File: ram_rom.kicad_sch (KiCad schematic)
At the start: 1 part

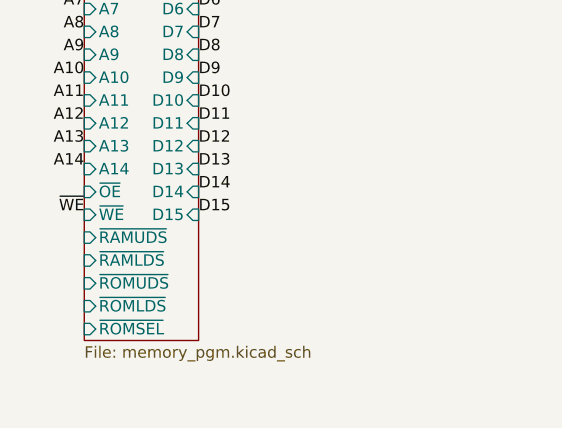
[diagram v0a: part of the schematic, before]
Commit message: Switch ROM chips to SRAM and add onboard programmer
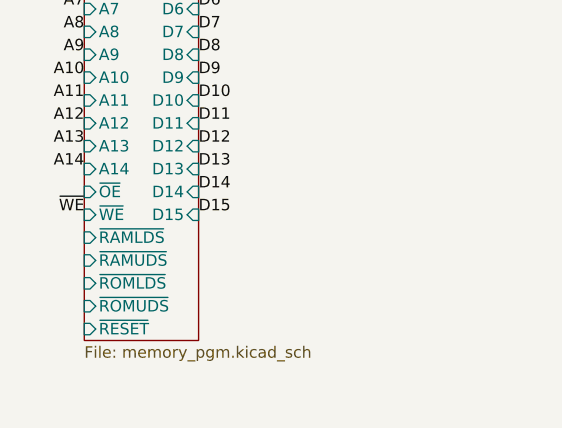
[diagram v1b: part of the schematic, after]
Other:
- sheet MemoryPgm ports: added ~{RESET}; removed ~{ROMSEL}

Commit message: Add title and rev number
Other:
- title: (none) -> RAM/ROM Board
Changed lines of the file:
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@@
 (kicad_sch (version 20211123) (generator eeschema)
   (paper "USLetter")
+  (title_block
+    (title "RAM/ROM Board")
+    (rev "1")
+  )
   (label "D9" (at 238.76 120.65 180)
     (effects (font (size 1.27 1.27)) (justify right bottom))

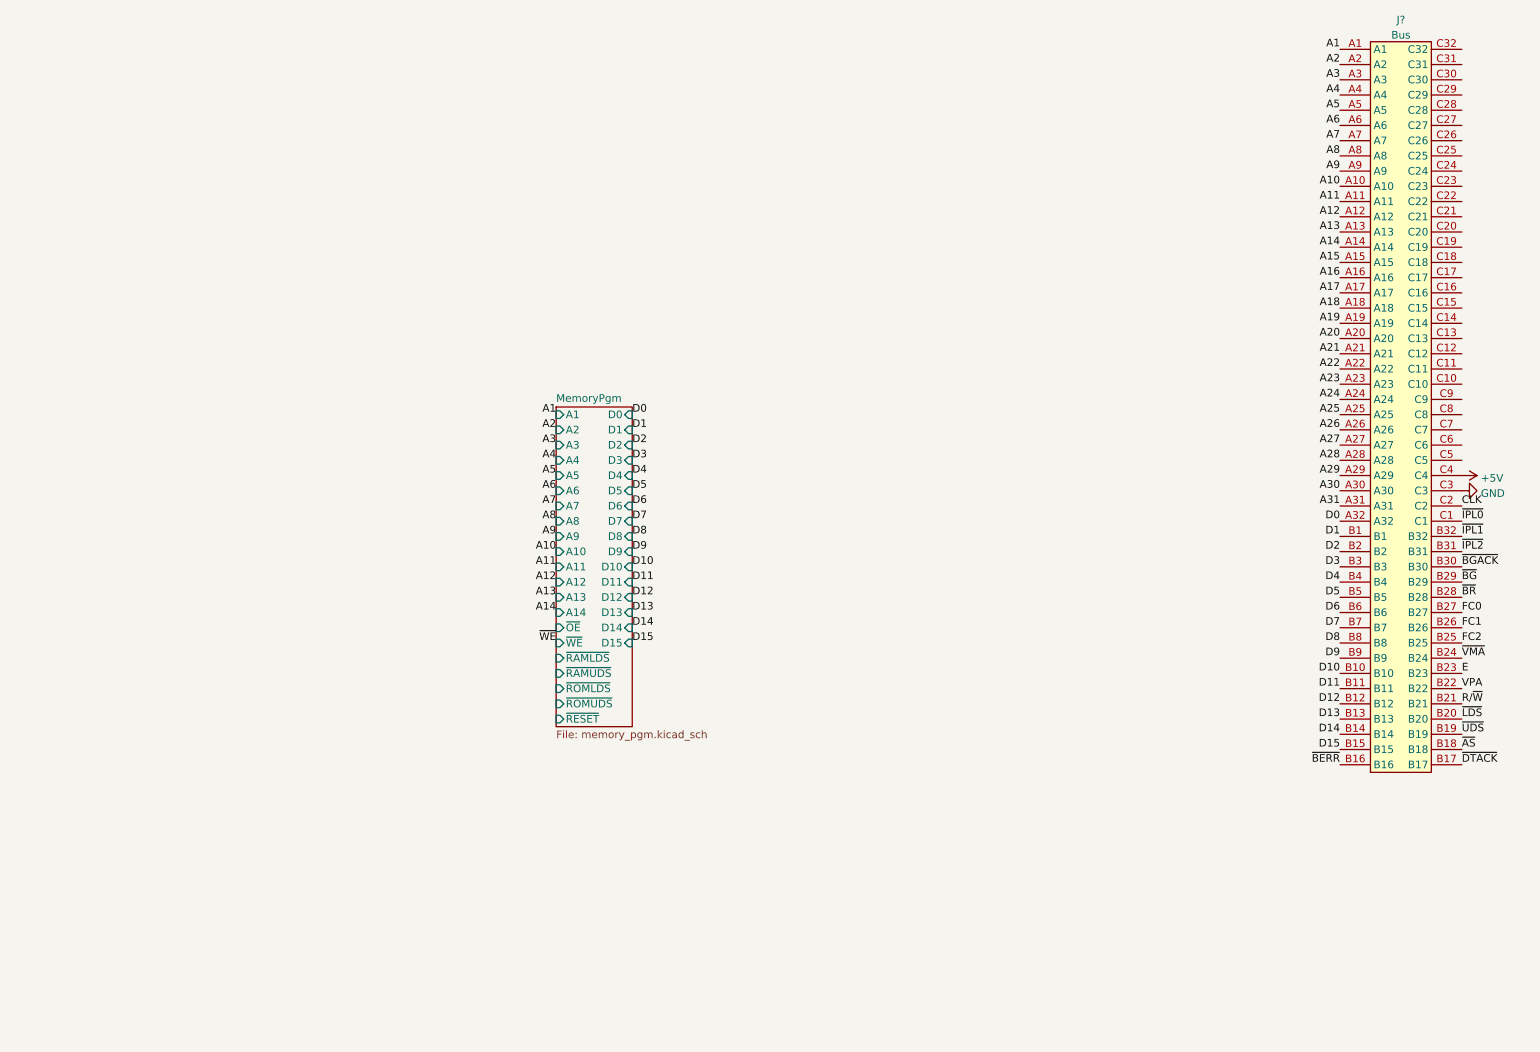
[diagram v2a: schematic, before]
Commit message: First pass at address decoding logic
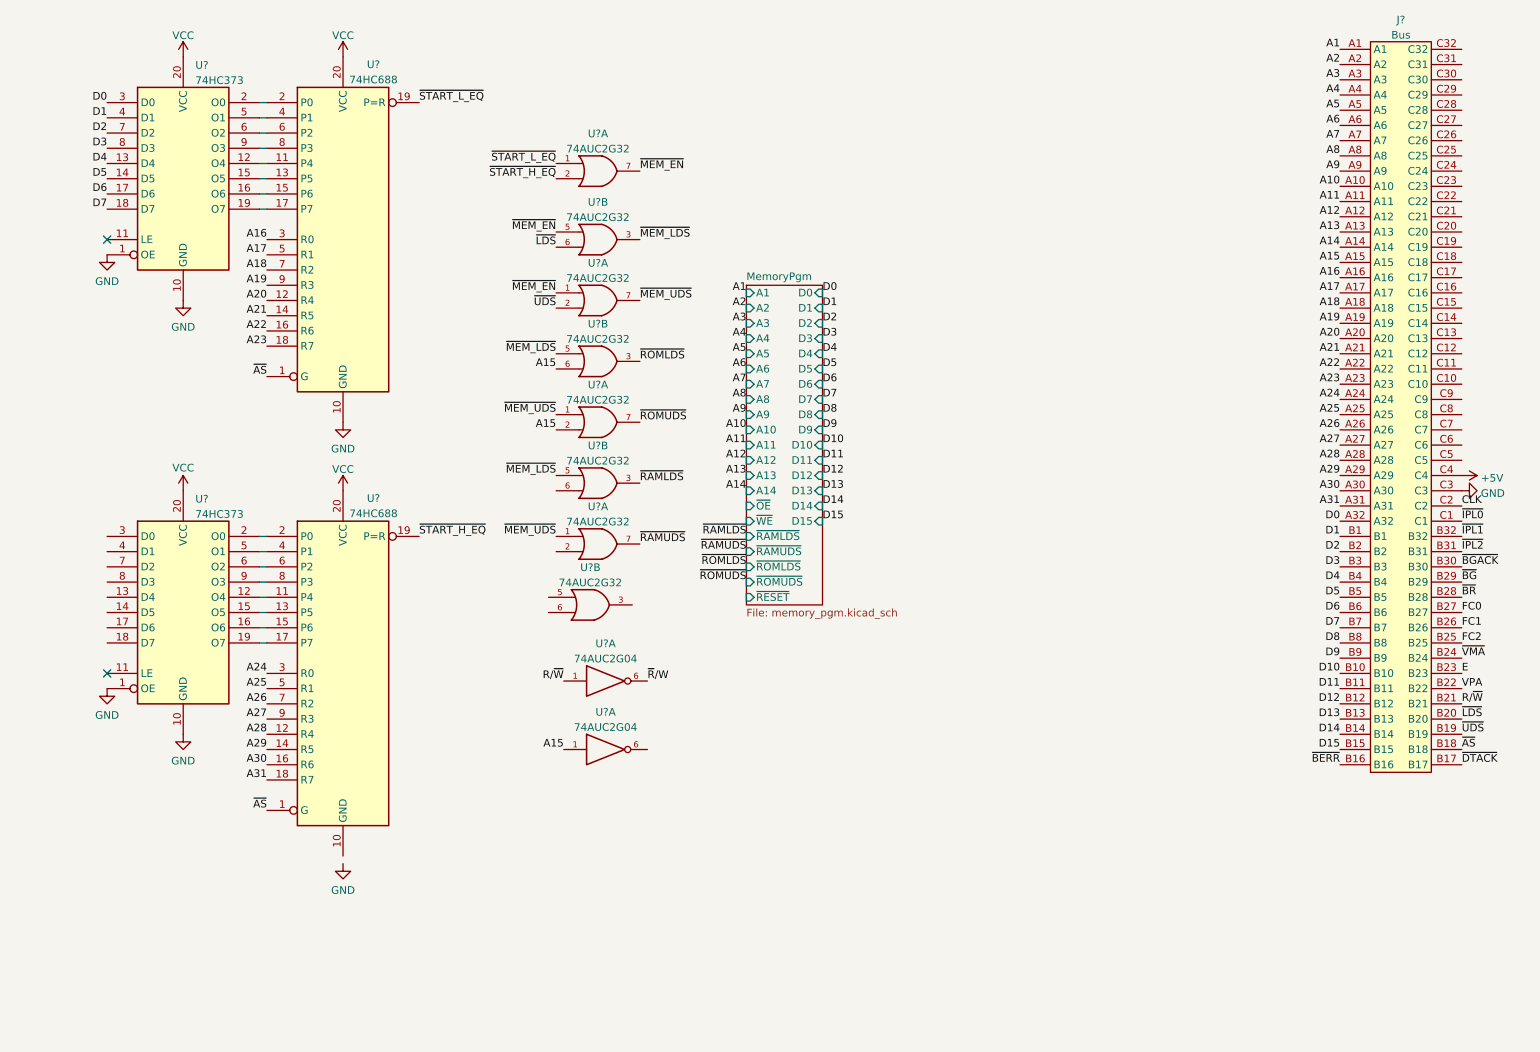
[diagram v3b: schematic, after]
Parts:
- added U? (x8): 74AUC2G32, symbol 74xGxx:74AUC2G32
- added U? (x2): 74AUC2G04, symbol 74xGxx:74AUC2G04
- added U? (x2): 74HC688, symbol 74xx:74HC688
- added U? (x2): 74HC373, symbol 74xx:74HC373
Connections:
- net A15: now also U?.1, U?.2, U?.6
- net A16: now also U?.3 (R0)
- net A17: now also U?.5 (R1)
- net A18: now also U?.7 (R2)
- net A19: now also U?.9 (R3)
- net A20: now also U?.12 (R4)
- net A21: now also U?.14 (R5)
- net A22: now also U?.16 (R6)
- net A23: now also U?.18 (R7)
- net A24: now also U?.3 (R0)
- net A25: now also U?.5 (R1)
- net A26: now also U?.7 (R2)
- net A27: now also U?.9 (R3)
- net A28: now also U?.12 (R4)
- net A29: now also U?.14 (R5)
- net A30: now also U?.16 (R6)
- net A31: now also U?.18 (R7)
- net D0: now also U?.3 (D0)
- net D1: now also U?.4 (D1)
- net D2: now also U?.7 (D2)
- net D3: now also U?.8 (D3)
- net D4: now also U?.13 (D4)
- net D5: now also U?.14 (D5)
- net D6: now also U?.17 (D6)
- net D7: now also U?.18 (D7)
- net GND: now also U?.1 (OE), U?.1 (OE), U?.10 (GND), U?.10 (GND), U?.10 (GND), U?.2 (GND), U?.2 (GND), U?.4 (GND), U?.4 (GND), U?.4 (GND), U?.4 (GND), U?.4 (GND), U?.4 (GND), U?.4 (GND), U?.4 (GND)
- net R/~{W}: now also U?.1
- net ~{AS}: now also U?.1 (G), U?.1 (G)
- net ~{LDS}: now also U?.6
- net ~{UDS}: now also U?.2
- new net: U?.11 (P4), U?.12 (O4) (x2)
- new net: U?.13 (P5), U?.15 (O5) (x2)
- new net: U?.15 (P6), U?.16 (O6) (x2)
- new net: U?.17 (P7), U?.19 (O7) (x2)
- new net: U?.2 (O0), U?.2 (P0) (x2)
- new net: U?.4 (P1), U?.5 (O1) (x2)
- new net: U?.6 (O2), U?.6 (P2) (x2)
- new net: U?.8 (P3), U?.9 (O3) (x2)
- new net VCC: U?.20 (VCC), U?.20 (VCC), U?.20 (VCC), U?.20 (VCC), U?.5 (VCC), U?.5 (VCC), U?.8 (VCC), U?.8 (VCC), U?.8 (VCC), U?.8 (VCC), U?.8 (VCC), U?.8 (VCC), U?.8 (VCC), U?.8 (VCC)
- new net ~{MEM_EN}: U?.1, U?.5, U?.7
- new net ~{MEM_LDS}: U?.3, U?.5, U?.5
- new net ~{MEM_UDS}: U?.1, U?.1, U?.7
- new net ~{RAMLDS}: U?.3
- new net ~{RAMUDS}: U?.7
- new net ~{ROMLDS}: U?.3
- new net ~{ROMUDS}: U?.7
- new net ~{R}/W: U?.6
- new net ~{START_H_EQ}: U?.19 (P=R), U?.2
- new net ~{START_L_EQ}: U?.1, U?.19 (P=R)
- no-connect marks 0 -> 2

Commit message: Consolidate RAM into one chip and work on adddress decoding
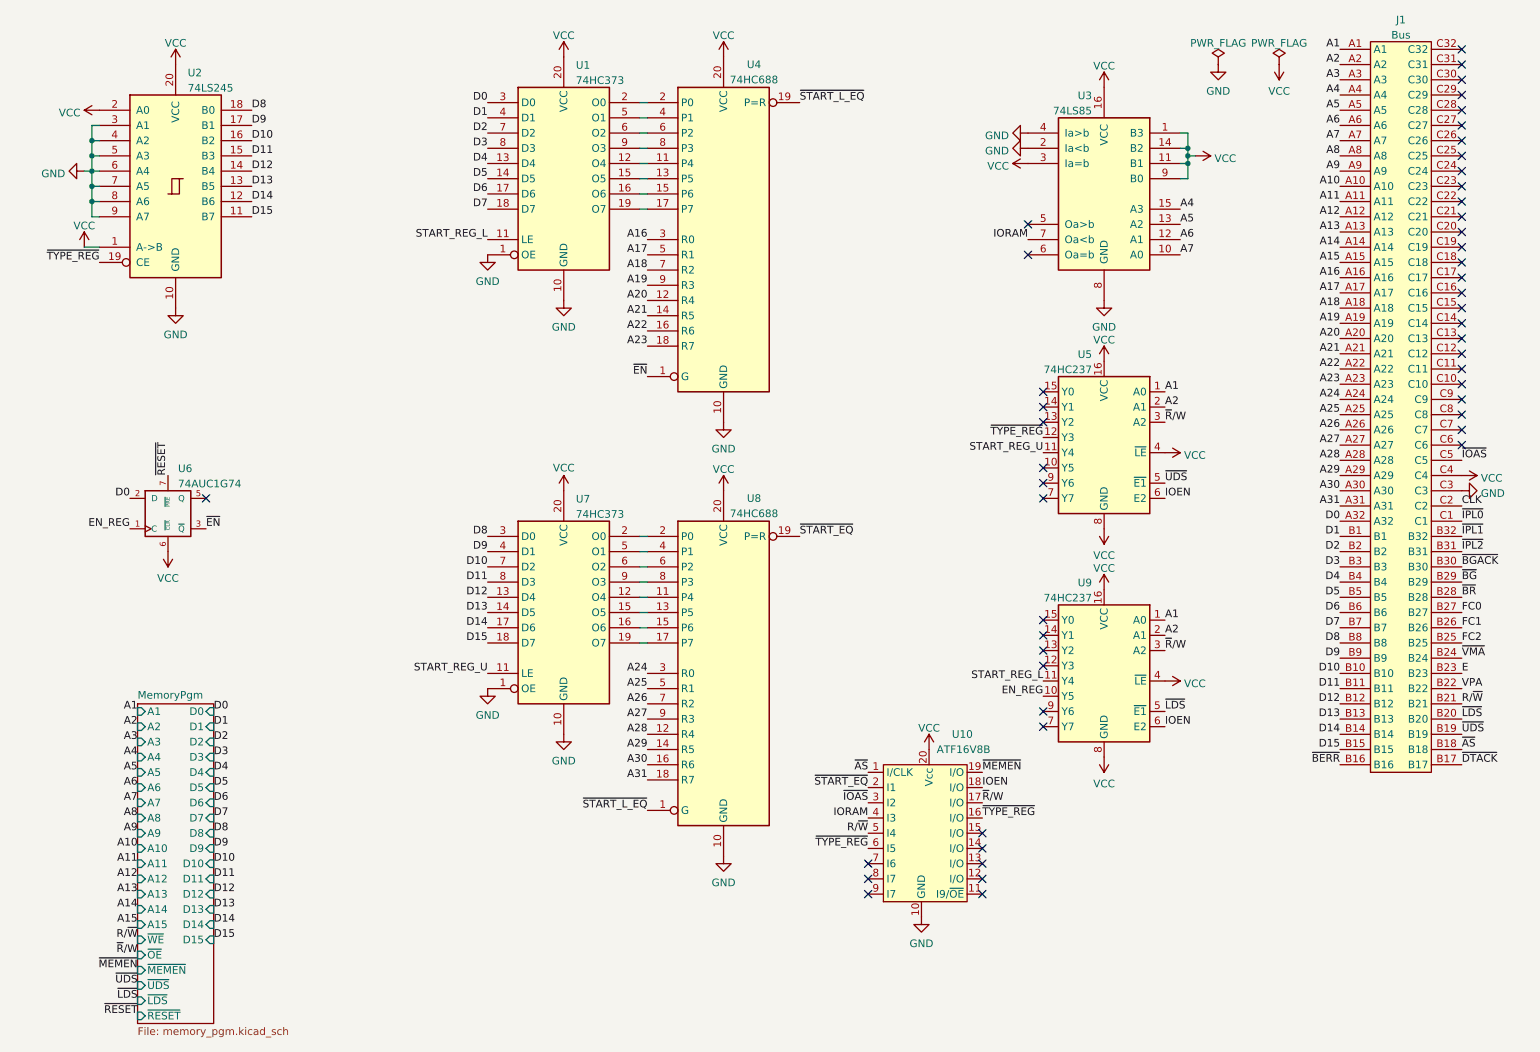
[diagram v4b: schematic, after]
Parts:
- removed U? (x8): 74AUC2G32, symbol 74xGxx:74AUC2G32
- removed U? (x2): 74AUC2G04, symbol 74xGxx:74AUC2G04
- added U10: ATF16V8B, symbol parts:ATF16V8B
- added U2: 74LS245, symbol 74xx:74LS245
- added U3: 74LS85, symbol 74xx:74LS85
- added U5, U9: 74HC237, symbol 74xx:74HC237
- added U6: 74AUC1G74, symbol 74xGxx:74AUC1G74
- gave numbers to parts that had none: 5
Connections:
- net +5V is gone; now on net VCC: J1.C4
- net A1: now also U5.1 (A0), U9.1 (A0)
- net A2: now also U5.2 (A1), U9.2 (A1)
- net A4: now also U3.15 (A3)
- net A5: now also U3.13 (A2)
- net A6: now also U3.12 (A1)
- net A7: now also U3.10 (A0)
- net D0: now also U6.2 (D)
- net D10: now also U7.7 (D2), U2.16 (B2)
- net D11: now also U7.8 (D3), U2.15 (B3)
- net D12: now also U7.13 (D4), U2.14 (B4)
- net D13: now also U7.14 (D5), U2.13 (B5)
- net D14: now also U7.17 (D6), U2.12 (B6)
- net D15: now also U7.18 (D7), U2.11 (B7)
- net D8: now also U7.3 (D0), U2.18 (B0)
- net D9: now also U7.4 (D1), U2.17 (B1)
- net GND: now also U8.10 (GND), U10.10 (GND), U2.10 (GND), U2.3 (A1), U2.4 (A2), U2.5 (A3), U2.6 (A4), U2.7 (A5), U2.8 (A6), U2.9 (A7), U3.2 (Ia<b), U3.4 (Ia>b), U3.8 (GND), U6.4 (GND)
- net R/~{W}: now also U10.5 (I4)
- net VCC: now also U10.20 (Vcc), U2.1 (A->B), U2.2 (A0), U2.20 (VCC), U3.1 (B3), U3.11 (B1), U3.14 (B2), U3.16 (VCC), U3.3 (Ia=b), U3.9 (B0), U5.16 (VCC), U5.4 (~{LE}), U5.8 (GND), U6.6 (~{CLR}), U6.8 (VCC), U9.16 (VCC), U9.4 (~{LE}), U9.8 (GND)
- net ~{AS}: now also U10.1 (I/CLK); no longer U4.1 (G), U8.1 (G)
- net ~{LDS}: now also U9.5 (~{E1})
- net ~{R}/W: now also U10.17 (I/O), U5.3 (A2), U9.3 (A2)
- net ~{START_L_EQ}: now also U8.1 (G)
- net ~{UDS}: now also U5.5 (~{E1})
- net ~{IOAS}: now reaches J1.C5
- net ~{IOAS}: now also U10.3 (I2)
- net START_REG_U: now reaches U7.11 (LE)
- net START_REG_U: now also U5.11 (Y4)
- net START_REG_L: now reaches U1.11 (LE)
- net START_REG_L: now also U9.11 (Y4)
- net ~{START_H_EQ} renamed ~{START_EQ}
- net ~{START_EQ}: now also U10.2 (I1)
- new net EN_REG: U6.1 (C), U9.10 (Y5)
- new net IOEN: U10.18 (I/O), U5.6 (E2), U9.6 (E2)
- new net IORAM: U10.4 (I3), U3.7 (Oa<b)
- new net ~{EN}: U4.1 (G), U6.3 (~{Q})
- new net ~{MEMEN}: U10.19 (I/O)
- new net ~{RESET}: U6.7 (~{PRE})
- new net ~{TYPE_REG}: U10.16 (I/O), U10.6 (I5), U2.19 (CE), U5.12 (Y3)
- no-connect marks 2 -> 50
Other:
- sheet MemoryPgm ports: added A15, ~{LDS}, ~{MEMEN}, ~{UDS}; removed ~{RAMLDS}, ~{RAMUDS}, ~{ROMLDS}, ~{ROMUDS}
- moved on the sheet: U1, U4, U7, U8
